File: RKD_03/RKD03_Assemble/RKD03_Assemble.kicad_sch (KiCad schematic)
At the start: 29 parts, among them J1 GROVE-CONNECTOR-DIP_4P-2.0_, SW1 RotaryEncoder_Switch, SW10 SW_Push, SW2 SW_Push, SW3 RotaryEncoder_Switch, SW4 SW_Push, SW5 RotaryEncoder_Switch, SW6 SW_Push, SW7 RotaryEncoder_Switch, SW8 SW_Push, SW9 RotaryEncoder_Switch, U1 Pico

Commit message: LEDの誤り修正1.01
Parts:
- LED1, LED2, LED3, LED4, LED5: footprint BrownSugar_KBD:RGBLED_SK6812MINI-E -> kbd_Parts:LED_SK6812MINI-E_BL
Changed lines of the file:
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@@
 			)
 		)
-		(property "Footprint" "BrownSugar_KBD:RGBLED_SK6812MINI-E"
+		(property "Footprint" "kbd_Parts:LED_SK6812MINI-E_BL"
 			(at 171.45 66.04 0)
 			(effects
@@
 			)
 		)
-		(property "Footprint" "BrownSugar_KBD:RGBLED_SK6812MINI-E"
+		(property "Footprint" "kbd_Parts:LED_SK6812MINI-E_BL"
 			(at 171.45 142.24 0)
 			(effects
@@
 			)
 		)
-		(property "Footprint" "BrownSugar_KBD:RGBLED_SK6812MINI-E"
+		(property "Footprint" "kbd_Parts:LED_SK6812MINI-E_BL"
 			(at 171.45 167.64 0)
 			(effects
@@
 			)
 		)
-		(property "Footprint" "BrownSugar_KBD:RGBLED_SK6812MINI-E"
+		(property "Footprint" "kbd_Parts:LED_SK6812MINI-E_BL"
 			(at 171.45 91.44 0)
 			(effects
@@
 			)
 		)
-		(property "Footprint" "BrownSugar_KBD:RGBLED_SK6812MINI-E"
+		(property "Footprint" "kbd_Parts:LED_SK6812MINI-E_BL"
 			(at 171.45 116.84 0)
 			(effects

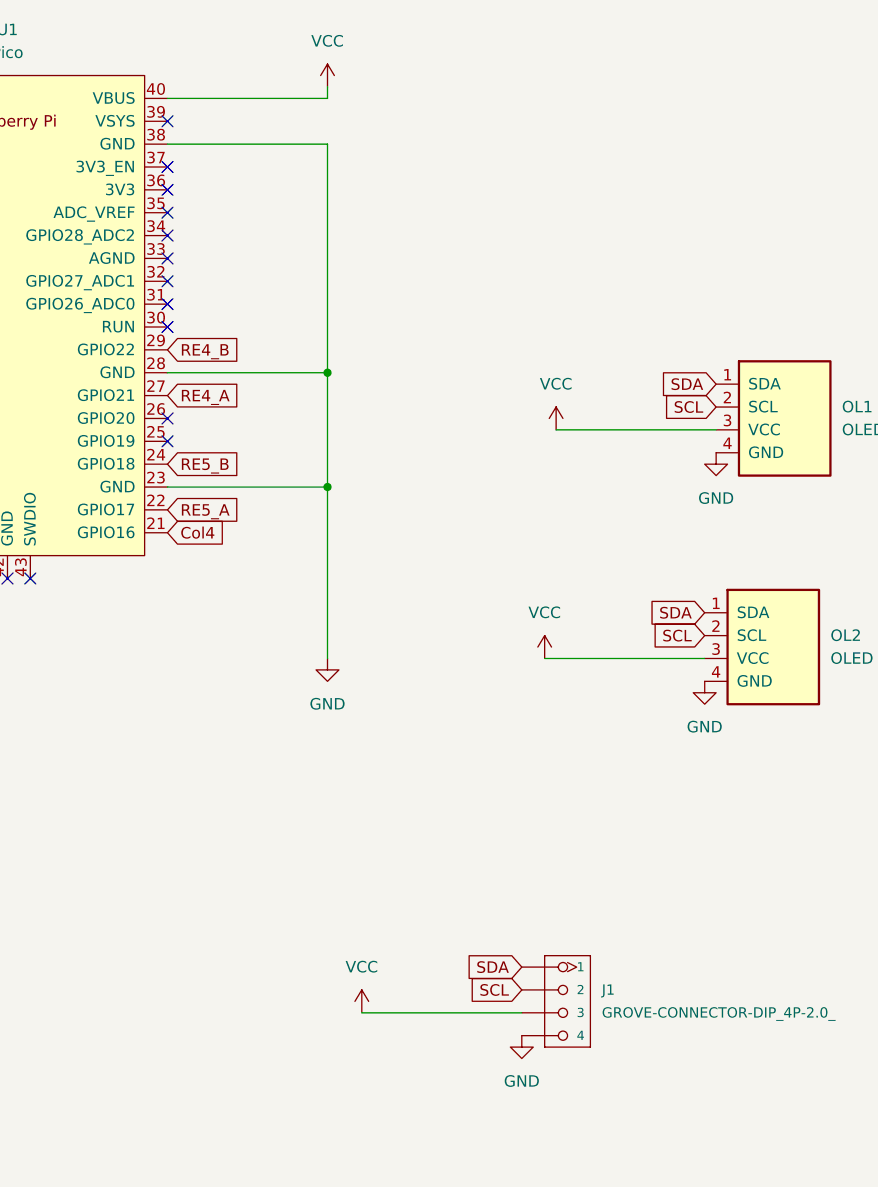
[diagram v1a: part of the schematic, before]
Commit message: I2Cの入力を3.3Vに修正
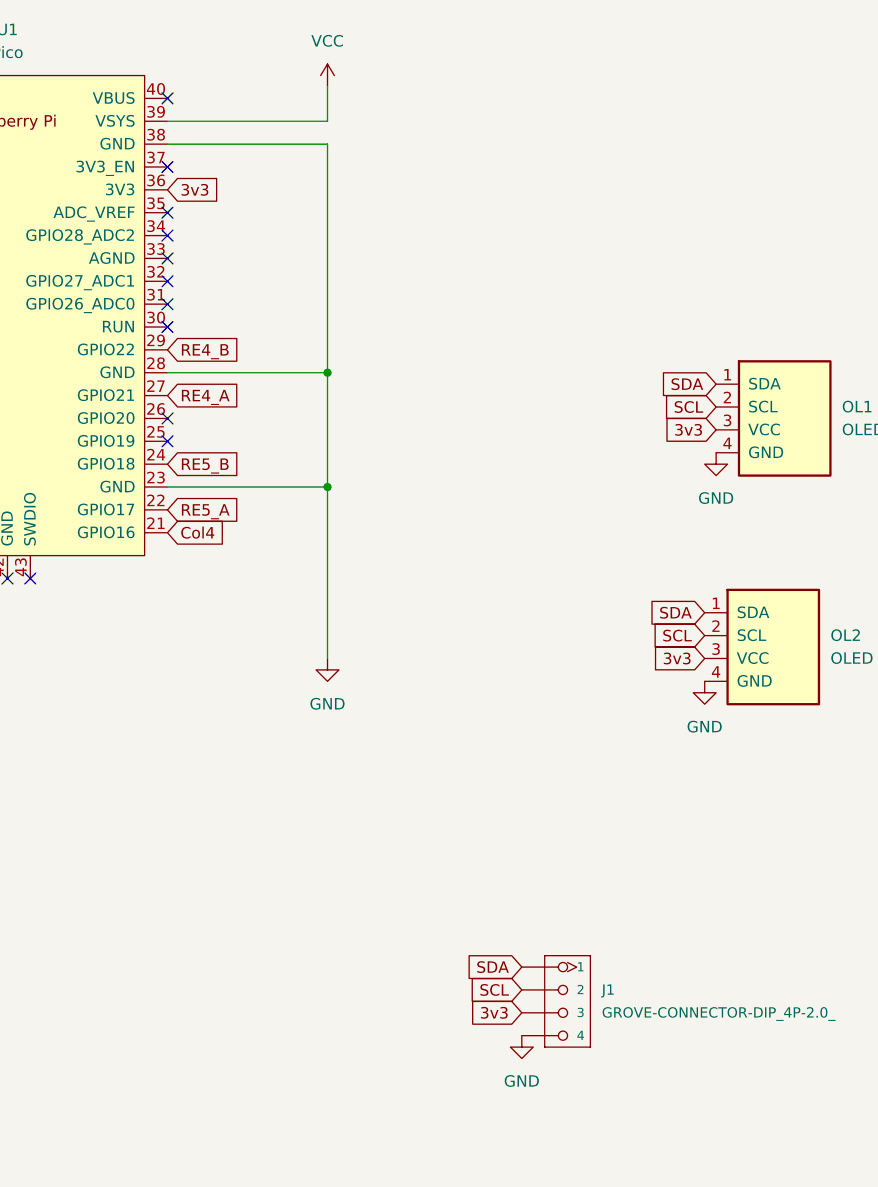
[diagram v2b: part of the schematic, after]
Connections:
- net VCC: now also U1.39 (VSYS); no longer J1.3, OL1.3 (VCC), OL2.3 (VCC), U1.40 (VBUS)
- net 3v3: now reaches U1.36 (3V3)
- net 3v3: now also J1.3, OL1.3 (VCC), OL2.3 (VCC)
- no-connect marks 16 -> 15
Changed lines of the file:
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@@
 	)
 	(no_connect
-		(at 83.82 29.21)
-	)
-	(no_connect
 		(at 83.82 46.99)
 	)
@@
 	)
 	(no_connect
-		(at 83.82 36.83)
+		(at 83.82 26.67)
 	)
 	(no_connect
@@
 	(wire
 		(pts
-			(xy 125.73 88.9) (xy 143.51 88.9)
-		)
-		(stroke
-			(width 0)
-			(type default)
-		)
-	)
-	(wire
-		(pts
 			(xy 185.42 139.7) (xy 185.42 114.3)
 		)
@@
 	(wire
 		(pts
-			(xy 105.41 128.27) (xy 123.19 128.27)
-		)
-		(stroke
-			(width 0)
-			(type default)
-		)
-	)
-	(wire
-		(pts
 			(xy 185.42 165.1) (xy 185.42 139.7)
 		)
@@
 	(wire
 		(pts
-			(xy 38.1 241.3) (xy 60.96 241.3)
+			(xy 83.82 29.21) (xy 101.6 29.21)
 		)
 		(stroke
@@
 	(wire
 		(pts
-			(xy 83.82 69.85) (xy 101.6 69.85)
+			(xy 38.1 241.3) (xy 60.96 241.3)
 		)
 		(stroke
@@
 	(wire
 		(pts
-			(xy 160.02 217.17) (xy 160.02 218.44)
+			(xy 83.82 69.85) (xy 101.6 69.85)
 		)
 		(stroke
@@
 	(wire
 		(pts
-			(xy 86.36 241.3) (xy 111.76 241.3)
+			(xy 160.02 217.17) (xy 160.02 218.44)
 		)
 		(stroke
@@
 	(wire
 		(pts
-			(xy 83.82 218.44) (xy 83.82 217.17)
+			(xy 86.36 241.3) (xy 111.76 241.3)
 		)
 		(stroke
@@
 	(wire
 		(pts
-			(xy 83.82 26.67) (xy 101.6 26.67)
+			(xy 83.82 218.44) (xy 83.82 217.17)
 		)
 		(stroke
@@
 	(wire
 		(pts
-			(xy 101.6 26.67) (xy 101.6 25.4)
-		)
-		(stroke
-			(width 0)
-			(type default)
-		)
-	)
-	(wire
-		(pts
 			(xy 127 233.68) (xy 132.08 233.68)
 		)
@@
 	(wire
 		(pts
-			(xy 177.8 71.12) (xy 177.8 81.28)
+			(xy 101.6 25.4) (xy 101.6 29.21)
 		)
 		(stroke
@@
 	(wire
 		(pts
-			(xy 111.76 241.3) (xy 137.16 241.3)
+			(xy 177.8 71.12) (xy 177.8 81.28)
 		)
 		(stroke
@@
 	(wire
 		(pts
-			(xy 127 63.5) (xy 144.78 63.5)
+			(xy 111.76 241.3) (xy 137.16 241.3)
 		)
 		(stroke
@@
 		)
 	)
+	(global_label "3v3"
+		(shape input)
+		(at 144.78 63.5 180)
+		(fields_autoplaced yes)
+		(effects
+			(font
+				(size 1.27 1.27)
+			)
+			(justify right)
+		)
+		(property "Intersheetrefs" "${INTERSHEET_REFS}"
+			(at 138.4082 63.5 0)
+			(effects
+				(font
+					(size 1.27 1.27)
+				)
+				(justify right)
+				(hide yes)
+			)
+		)
+	)
 	(global_label "SCL"
 		(shape input)
@@
 		)
 	)
+	(global_label "3v3"
+		(shape input)
+		(at 143.51 88.9 180)
+		(fields_autoplaced yes)
+		(effects
+			(font
+				(size 1.27 1.27)
+			)
+			(justify right)
+		)
+		(property "Intersheetrefs" "${INTERSHEET_REFS}"
+			(at 137.1382 88.9 0)
+			(effects
+				(font
+					(size 1.27 1.27)
+				)
+				(justify right)
+				(hide yes)
+			)
+		)
+	)
 	(global_label "RE1_B"
 		(shape input)
@@
 		)
 	)
+	(global_label "3v3"
+		(shape input)
+		(at 123.19 128.27 180)
+		(fields_autoplaced yes)
+		(effects
+			(font
+				(size 1.27 1.27)
+			)
+			(justify right)
+		)
+		(property "Intersheetrefs" "${INTERSHEET_REFS}"
+			(at 116.8182 128.27 0)
+			(effects
+				(font
+					(size 1.27 1.27)
+				)
+				(justify right)
+				(hide yes)
+			)
+		)
+	)
 	(global_label "RE2_A"
 		(shape input)
@@
 		)
 	)
+	(global_label "3v3"
+		(shape input)
+		(at 83.82 36.83 0)
+		(fields_autoplaced yes)
+		(effects
+			(font
+				(size 1.27 1.27)
+			)
+			(justify left)
+		)
+		(property "Intersheetrefs" "${INTERSHEET_REFS}"
+			(at 90.1918 36.83 0)
+			(effects
+				(font
+					(size 1.27 1.27)
+				)
+				(justify left)
+				(hide yes)
+			)
+		)
+	)
 	(global_label "LED"
 		(shape input)
@@
 	)
 	(symbol
-		(lib_id "power:VCC")
-		(at 125.73 88.9 0)
-		(unit 1)
-		(exclude_from_sim no)
-		(in_bom yes)
-		(on_board yes)
-		(dnp no)
-		(fields_autoplaced yes)
-		(property "Reference" "#PWR08"
-			(at 125.73 92.71 0)
-			(effects
-				(font
-					(size 1.27 1.27)
-				)
-				(hide yes)
-			)
-		)
-		(property "Value" "VCC"
-			(at 125.73 83.82 0)
-			(effects
-				(font
-					(size 1.27 1.27)
-				)
-			)
-		)
-		(property "Footprint" ""
-			(at 125.73 88.9 0)
-			(effects
-				(font
-					(size 1.27 1.27)
-				)
-				(hide yes)
-			)
-		)
-		(property "Datasheet" ""
-			(at 125.73 88.9 0)
-			(effects
-				(font
-					(size 1.27 1.27)
-				)
-				(hide yes)
-			)
-		)
-		(property "Description" "Power symbol creates a global label with name \"VCC\""
-			(at 125.73 88.9 0)
-			(effects
-				(font
-					(size 1.27 1.27)
-				)
-				(hide yes)
-			)
-		)
-		(pin "1"
-		)
-		(instances
-			(project "RKD03_Assemble"
-				(path "/32b3db6f-ec5a-43c8-b598-c76dc9760296"
-					(reference "#PWR08")
-					(unit 1)
-				)
-			)
-		)
-	)
-	(symbol
 		(lib_id "Device:D")
 		(at 66.04 262.89 90)
@@
 					(unit 1)
 				)
-			)
-		)
-	)
-	(symbol
-		(lib_id "power:VCC")
-		(at 105.41 128.27 0)
-		(unit 1)
-		(exclude_from_sim no)
-		(in_bom yes)
-		(on_board yes)
-		(dnp no)
-		(fields_autoplaced yes)
-		(property "Reference" "#PWR013"
-			(at 105.41 132.08 0)
-			(effects
-				(font
-					(size 1.27 1.27)
-				)
-				(hide yes)
-			)
-		)
-		(property "Value" "VCC"
-			(at 105.41 123.19 0)
-			(effects
-				(font
-					(size 1.27 1.27)
-				)
-			)
-		)
-		(property "Footprint" ""
-			(at 105.41 128.27 0)
-			(effects
-				(font
-					(size 1.27 1.27)
-				)
-				(hide yes)
-			)
-		)
-		(property "Datasheet" ""
-			(at 105.41 128.27 0)
-			(effects
-				(font
-					(size 1.27 1.27)
-				)
-				(hide yes)
-			)
-		)
-		(property "Description" "Power symbol creates a global label with name \"VCC\""
-			(at 105.41 128.27 0)
-			(effects
-				(font
-					(size 1.27 1.27)
-				)
-				(hide yes)
-			)
-		)
-		(pin "1"
-		)
-		(instances
-			(project "RKD03_Assemble"
-				(path "/32b3db6f-ec5a-43c8-b598-c76dc9760296"
-					(reference "#PWR013")
-					(unit 1)
-				)
-			)
-		)
-	)
-	(symbol
-		(lib_id "power:VCC")
-		(at 127 63.5 0)
-		(unit 1)
-		(exclude_from_sim no)
-		(in_bom yes)
-		(on_board yes)
-		(dnp no)
-		(fields_autoplaced yes)
-		(property "Reference" "#PWR09"
-			(at 127 67.31 0)
-			(effects
-				(font
-					(size 1.27 1.27)
-				)
-				(hide yes)
-			)
-		)
-		(property "Value" "VCC"
-			(at 127 58.42 0)
-			(effects
-				(font
-					(size 1.27 1.27)
-				)
-			)
-		)
-		(property "Footprint" ""
-			(at 127 63.5 0)
-			(effects
-				(font
-					(size 1.27 1.27)
-				)
-				(hide yes)
-			)
-		)
-		(property "Datasheet" ""
-			(at 127 63.5 0)
-			(effects
-				(font
-					(size 1.27 1.27)
-				)
-				(hide yes)
-			)
-		)
-		(property "Description" "Power symbol creates a global label with name \"VCC\""
-			(at 127 63.5 0)
-			(effects
-				(font
-					(size 1.27 1.27)
-				)
-				(hide yes)
-			)
-		)
-		(pin "1"
-		)
-		(instances
-			(project "RKD03_Assemble"
-				(path "/32b3db6f-ec5a-43c8-b598-c76dc9760296"
-					(reference "#PWR09")
-					(unit 1)
-				)

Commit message: RKD03V2作成中
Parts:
- added D1, D10, D13, D4, D7: D, kbd_Parts:Diode_SMD, symbol Device:D
- added SW1, SW10, SW13, SW4, SW7: SW_Push, kbd_SW:Choc_Hotswap_1u, symbol Switch:SW_Push
- renumbered D7 to D11, D8 to D12, D9 to D14, D10 to D15, D1 to D2, D2 to D3, D3 to D5, D4 to D6, D5 to D8, D6 to D9, SW7 to SW11, SW8 to SW12, SW9 to SW14, SW10 to SW15, SW1 to SW2, SW2 to SW3, SW3 to SW5, SW4 to SW6, SW5 to SW8, SW6 to SW9
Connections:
- net Col0: now also SW1.2
- net Col1: now also SW4.2
- net Col2: now also SW7.2
- net Col3: now also SW10.2
- net Col4: now also SW13.2
- net Row0: now also D1.1 (K), D10.1 (K), D13.1 (K), D4.1 (K), D7.1 (K); no longer D11.1 (K), D14.1 (K), D2.1 (K), D5.1 (K), D8.1 (K)
- net Row1: now also D11.1 (K), D14.1 (K), D2.1 (K), D5.1 (K), D8.1 (K); no longer D12.1 (K), D15.1 (K), D3.1 (K), D6.1 (K), D9.1 (K)
- net Row2: now reaches U1.15 (GPIO11)
- net Row2: now also D12.1 (K), D15.1 (K), D3.1 (K), D6.1 (K), D9.1 (K)
- new net: D10.2 (A), SW10.1
- new net: D7.2 (A), SW7.1
- new net: D1.2 (A), SW1.1
- new net: D13.2 (A), SW13.1
- new net: D4.2 (A), SW4.1
- no-connect marks 15 -> 14
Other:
- moved on the sheet: LED1, LED2, LED3, LED4, LED5

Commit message: RKD03_手直し
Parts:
- removed D15: D, kbd_Parts:Diode_SMD, symbol Device:D
- removed J1: GROVE-CONNECTOR-DIP_4P-2.0_, OPL_Connector:GROVE-HW4-2.0, symbol OPL_Connector:GROVE-CONNECTOR-DIP_4P-2.0_
- removed SW15: SW_Push, kbd_SW:Choc_Hotswap_1u, symbol Switch:SW_Push
- SW1, SW10, SW13, SW3, SW4, SW6, SW7, SW9: footprint kbd_SW:Choc_Hotswap_1u -> Rikkodo_FootPrint:rkd_Choc_v2_Hotswap_1u
- SW12: footprint kbd_SW:Choc_Hotswap_1u -> Rikkodo_FootPrint:rkd_Choc_v2_Hotswap_2u
- U1: footprint RPi_Pico:RPi_Pico_SMD_TH -> Rikkodo_FootPrint:rkd_RPi_Pico_TH

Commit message: RKD03 V1V2に修正
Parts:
- SW1, SW10, SW13, SW3, SW4, SW6, SW7, SW9: footprint Rikkodo_FootPrint:rkd_Choc_v2_Hotswap_1u -> Rikkodo_FootPrint:rkd_Choc_v1v2_Hotswap_1u
- SW12: footprint Rikkodo_FootPrint:rkd_Choc_v2_Hotswap_2u -> Rikkodo_FootPrint:rkd_Choc_v1v2_Hotswap_2u
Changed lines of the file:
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@@
 			)
 		)
-		(property "Footprint" "Rikkodo_FootPrint:rkd_Choc_v2_Hotswap_1u"
+		(property "Footprint" "Rikkodo_FootPrint:rkd_Choc_v1v2_Hotswap_1u"
 			(at 86.36 254 0)
 			(effects
@@
 			)
 		)
-		(property "Footprint" "Rikkodo_FootPrint:rkd_Choc_v2_Hotswap_1u"
+		(property "Footprint" "Rikkodo_FootPrint:rkd_Choc_v1v2_Hotswap_1u"
 			(at 55.88 181.61 0)
 			(effects
@@
 			)
 		)
-		(property "Footprint" "Rikkodo_FootPrint:rkd_Choc_v2_Hotswap_1u"
+		(property "Footprint" "Rikkodo_FootPrint:rkd_Choc_v1v2_Hotswap_1u"
 			(at 157.48 181.61 0)
 			(effects
@@
 			)
 		)
-		(property "Footprint" "Rikkodo_FootPrint:rkd_Choc_v2_Hotswap_1u"
+		(property "Footprint" "Rikkodo_FootPrint:rkd_Choc_v1v2_Hotswap_1u"
 			(at 81.28 181.61 0)
 			(effects
@@
 			)
 		)
-		(property "Footprint" "Rikkodo_FootPrint:rkd_Choc_v2_Hotswap_1u"
+		(property "Footprint" "Rikkodo_FootPrint:rkd_Choc_v1v2_Hotswap_1u"
 			(at 132.08 181.61 0)
 			(effects
@@
 			)
 		)
-		(property "Footprint" "Rikkodo_FootPrint:rkd_Choc_v2_Hotswap_2u"
+		(property "Footprint" "Rikkodo_FootPrint:rkd_Choc_v1v2_Hotswap_2u"
 			(at 137.16 254 0)
 			(effects
@@
 			)
 		)
-		(property "Footprint" "Rikkodo_FootPrint:rkd_Choc_v2_Hotswap_1u"
+		(property "Footprint" "Rikkodo_FootPrint:rkd_Choc_v1v2_Hotswap_1u"
 			(at 106.68 181.61 0)
 			(effects
@@
 			)
 		)
-		(property "Footprint" "Rikkodo_FootPrint:rkd_Choc_v2_Hotswap_1u"
+		(property "Footprint" "Rikkodo_FootPrint:rkd_Choc_v1v2_Hotswap_1u"
 			(at 111.76 254 0)
 			(effects
@@
 			)
 		)
-		(property "Footprint" "Rikkodo_FootPrint:rkd_Choc_v2_Hotswap_1u"
+		(property "Footprint" "Rikkodo_FootPrint:rkd_Choc_v1v2_Hotswap_1u"
 			(at 60.96 254 0)
 			(effects

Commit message: RKD03 新フットプリントの検証
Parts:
- SW12: footprint Rikkodo_FootPrint:rkd_Choc_v1v2_Hotswap_2u -> Rikkodo_FootPrint:rkd_Choc_v1v2_Hotswap_2u_Gat
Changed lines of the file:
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@@
 			)
 		)
-		(property "Footprint" "Rikkodo_FootPrint:rkd_Choc_v1v2_Hotswap_2u"
+		(property "Footprint" "Rikkodo_FootPrint:rkd_Choc_v1v2_Hotswap_2u_Gat"
 			(at 137.16 254 0)
 			(effects

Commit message: RKDV3 見直し
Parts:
- removed D1, D13, D4, D7: D, kbd_Parts:Diode_SMD, symbol Device:D
- removed SW11, SW14, SW2, SW5, SW8: RotaryEncoder_Switch, kbd_Parts:RotaryEncoder_EC12E, symbol Device:RotaryEncoder_Switch
- removed SW13, SW4: SW_Push, Rikkodo_FootPrint:rkd_Choc_v1v2_Hotswap_1u, symbol Switch:SW_Push
- added J1: GROVE-CONNECTOR-DIP_4P-2.0_, OPL_Connector:GROVE-HW4-2.0, symbol OPL_Connector:GROVE-CONNECTOR-DIP_4P-2.0_
- added SW3, SW5, SW9: SW_Push, Rikkodo_FootPrint:rkd_CherryChoc_v1v2_Hotswap_1u, symbol Switch:SW_Push
- SW1, SW10, SW7: footprint Rikkodo_FootPrint:rkd_Choc_v1v2_Hotswap_1u -> Rikkodo_FootPrint:rkd_CherryChoc_v1v2_Hotswap_1u
- SW2: renamed from SW3; footprint Rikkodo_FootPrint:rkd_Choc_v1v2_Hotswap_1u -> Rikkodo_FootPrint:rkd_CherryChoc_v1v2_Hotswap_1u
- SW4: renamed from SW6; footprint Rikkodo_FootPrint:rkd_Choc_v1v2_Hotswap_1u -> Rikkodo_FootPrint:rkd_CherryChoc_v1v2_Hotswap_1u
- SW6: renamed from SW9; footprint Rikkodo_FootPrint:rkd_Choc_v1v2_Hotswap_1u -> Rikkodo_FootPrint:rkd_CherryChoc_v1v2_Hotswap_1u
- SW8: renamed from SW12; footprint Rikkodo_FootPrint:rkd_Choc_v1v2_Hotswap_2u_Gat -> Rikkodo_FootPrint:rkd_CherryChoc_v1v2_Hotswap_1u
- U1: footprint Rikkodo_FootPrint:rkd_RPi_Pico_TH -> RPi_Pico:RPi_Pico_SMD_TH
- renumbered D2 to D1, D3 to D2, D5 to D3, D6 to D4, D8 to D5, D9 to D6, D11 to D7, D12 to D8, D14 to D9
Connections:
- net 3v3: now also U1.37 (3V3_EN), J1.3; no longer U1.36 (3V3)
- net Col1: now also SW3.2
- net Col2: now also SW5.2; no longer SW7.2
- net Col3: now also SW7.2; no longer SW10.2
- net Col4: now also SW10.2, SW9.2
- net GND: now also J1.4
- net Row0: now also D1.1 (K), D3.1 (K), D5.1 (K), D7.1 (K), D9.1 (K); no longer D10.1 (K)
- net Row1: now also D10.1 (K), D2.1 (K), D4.1 (K), D6.1 (K), D8.1 (K); no longer D1.1 (K), D3.1 (K), D5.1 (K), D7.1 (K), D9.1 (K)
- net SCL: now also J1.2
- net SDA: now also J1.1
- net VCC: now also U1.40 (VBUS); no longer U1.39 (VSYS)
- net at SW7.1: now also D7.2 (A)
- net at SW1.1: now also D1.2 (A)
- net at D5.2 (A): now also SW5.1
- net at D9.2 (A): now also SW9.1
- net at D3.2 (A): now also SW3.1
- net RE1_A: no longer names the net of U1.4 (GPIO2)
- net RE1_B: no longer names the net of U1.2 (GPIO1)
- net RE2_A: no longer names the net of U1.14 (GPIO10)
- net RE2_B: no longer names the net of U1.12 (GPIO9)
- net RE3_A: no longer names the net of U1.19 (GPIO14)
- net RE3_B: no longer names the net of U1.17 (GPIO13)
- net RE4_A: no longer names the net of U1.27 (GPIO21)
- net RE4_B: no longer names the net of U1.29 (GPIO22)
- net RE5_A: no longer names the net of U1.22 (GPIO17)
- net RE5_B: no longer names the net of U1.24 (GPIO18)
- removed net Row2: D2.1 (K), D4.1 (K), D6.1 (K), D8.1 (K), U1.15 (GPIO11)
- no-connect marks 14 -> 25
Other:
- moved on the sheet: LED1, LED2, LED3, LED4, LED5
